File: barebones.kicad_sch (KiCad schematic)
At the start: 0 parts

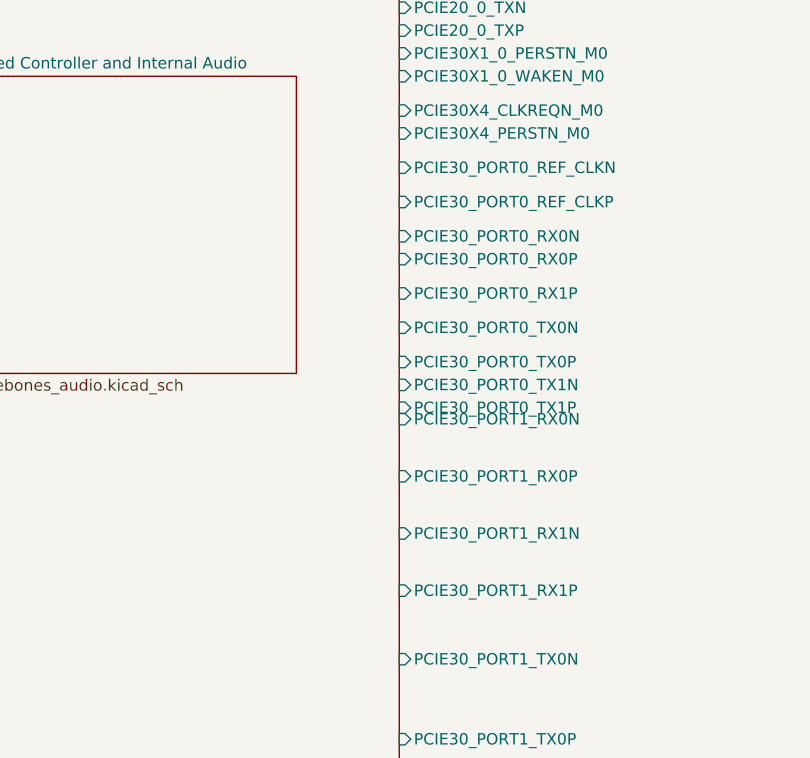
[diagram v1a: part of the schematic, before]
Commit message: added a USB 3.1 hub for the Type-A ports and a CLK generator for the PCIE 3.0/2.0
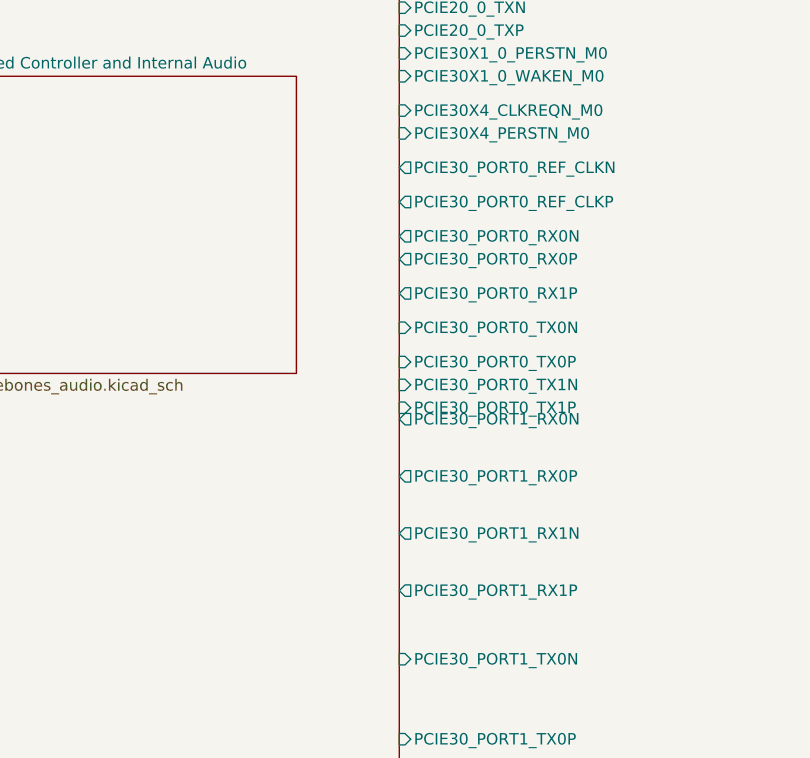
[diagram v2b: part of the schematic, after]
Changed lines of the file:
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@@
 			)
 		)
-		(pin "PCIE30_PORT0_REF_CLKN" input
+		(pin "PCIE30_PORT0_REF_CLKN" output
 			(at 172.72 166.37 180)
 			(effects
@@
 			)
 		)
-		(pin "PCIE30_PORT0_REF_CLKP" input
+		(pin "PCIE30_PORT0_REF_CLKP" output
 			(at 172.72 170.18 180)
 			(effects
@@
 			)
 		)
-		(pin "PCIE30_PORT0_RX0N" input
+		(pin "PCIE30_PORT0_RX0N" output
 			(at 172.72 173.99 180)
 			(effects
@@
 			)
 		)
-		(pin "PCIE30_PORT0_RX0P" input
+		(pin "PCIE30_PORT0_RX0P" output
 			(at 172.72 176.53 180)
 			(effects
@@
 			)
 		)
-		(pin "PCIE30_PORT0_RX1P" input
+		(pin "PCIE30_PORT0_RX1P" output
 			(at 172.72 180.34 180)
 			(effects
@@
 			)
 		)
-		(pin "PCIE30_PORT1_RX0N" input
+		(pin "PCIE30_PORT1_RX0N" output
 			(at 172.72 194.31 180)
 			(effects
@@
 			)
 		)
-		(pin "PCIE30_PORT1_RX0P" input
+		(pin "PCIE30_PORT1_RX0P" output
 			(at 172.72 200.66 180)
 			(effects
@@
 			)
 		)
-		(pin "PCIE30_PORT1_RX1N" input
+		(pin "PCIE30_PORT1_RX1N" output
 			(at 172.72 207.01 180)
 			(effects
@@
 			)
 		)
-		(pin "PCIE30_PORT1_RX1P" input
+		(pin "PCIE30_PORT1_RX1P" output
 			(at 172.72 213.36 180)
 			(effects

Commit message: added the display connector and its 12V power supply
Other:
- sheet High Speed IO ports: added DDR_CH0_A0_A, DDR_CH0_A0_B, DDR_CH0_A1_A, DDR_CH0_A1_B, DDR_CH0_A2_A, DDR_CH0_A2_B, DDR_CH0_A3_A, DDR_CH0_A3_B, DDR_CH0_A4_A, DDR_CH0_A4_B, DDR_CH0_A5_A, DDR_CH0_A5_B, DDR_CH0_CKB_A, DDR_CH0_CKB_B, DDR_CH0_CK_A, DDR_CH0_CK_B, DDR_CH0_DM0_A, DDR_CH0_DM0_B, DDR_CH0_DM1_A, DDR_CH0_DM1_B, DDR_CH0_DQ0_A, DDR_CH0_DQ0_B, DDR_CH0_DQ10_A, DDR_CH0_DQ10_B, DDR_CH0_DQ11_A, DDR_CH0_DQ11_B, DDR_CH0_DQ12_A, DDR_CH0_DQ12_B, DDR_CH0_DQ13_A, DDR_CH0_DQ13_B, DDR_CH0_DQ14_A, DDR_CH0_DQ14_B, DDR_CH0_DQ15_A, DDR_CH0_DQ15_B, DDR_CH0_DQ1_A, DDR_CH0_DQ1_B, DDR_CH0_DQ2_A, DDR_CH0_DQ2_B, DDR_CH0_DQ3_A, DDR_CH0_DQ3_B, DDR_CH0_DQ4_A, DDR_CH0_DQ4_B, DDR_CH0_DQ5_A, DDR_CH0_DQ5_B, DDR_CH0_DQ6_A, DDR_CH0_DQ6_B, DDR_CH0_DQ7_A, DDR_CH0_DQ7_B, DDR_CH0_DQ8_A, DDR_CH0_DQ8_B, DDR_CH0_DQ9_A, DDR_CH0_DQ9_B, DDR_CH0_DQS0N_A, DDR_CH0_DQS0N_B, DDR_CH0_DQS0P_A, DDR_CH0_DQS0P_B, DDR_CH0_DQS1N_A, DDR_CH0_DQS1N_B, DDR_CH0_DQS1P_A, DDR_CH0_DQS1P_B, DDR_CH0_LP4/4X_CKE0/LP5_CS0_A, DDR_CH0_LP4/4X_CKE0/LP5_CS0_B, DDR_CH0_LP4/4X_CKE1/LP5_CS1_A, DDR_CH0_LP4/4X_CKE1/LP5_CS1_B, DDR_CH0_LP4/4X_CS0_A, DDR_CH0_LP4/4X_CS0_B, DDR_CH0_LP4/4X_CS1_A, DDR_CH0_LP4/4X_CS1_B, DDR_CH1_A0_C, DDR_CH1_A0_D, DDR_CH1_A1_C, DDR_CH1_A1_D, DDR_CH1_A2_C, DDR_CH1_A2_D, DDR_CH1_A3_C, DDR_CH1_A3_D, DDR_CH1_A4_C, DDR_CH1_A4_D, DDR_CH1_A5_C, DDR_CH1_A5_D, DDR_CH1_CKB_C, DDR_CH1_CKB_D; removed none
